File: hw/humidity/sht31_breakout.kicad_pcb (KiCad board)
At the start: 2 copper layers, 17.8 x 15.2 mm, 8 parts, among them P1 CONN_01X06, U1 SHT3x-DIS

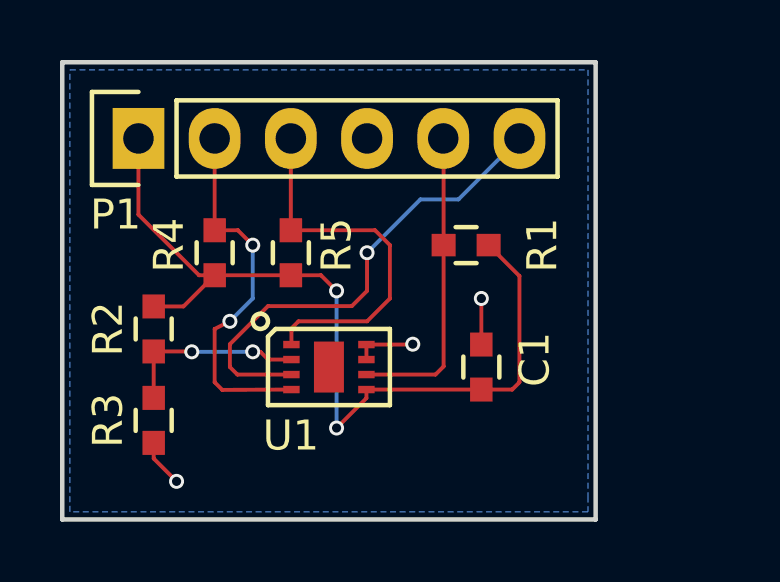
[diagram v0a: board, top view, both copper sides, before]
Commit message: Made much smaller SHT31 breakout
We'll see if I can hand solder it...
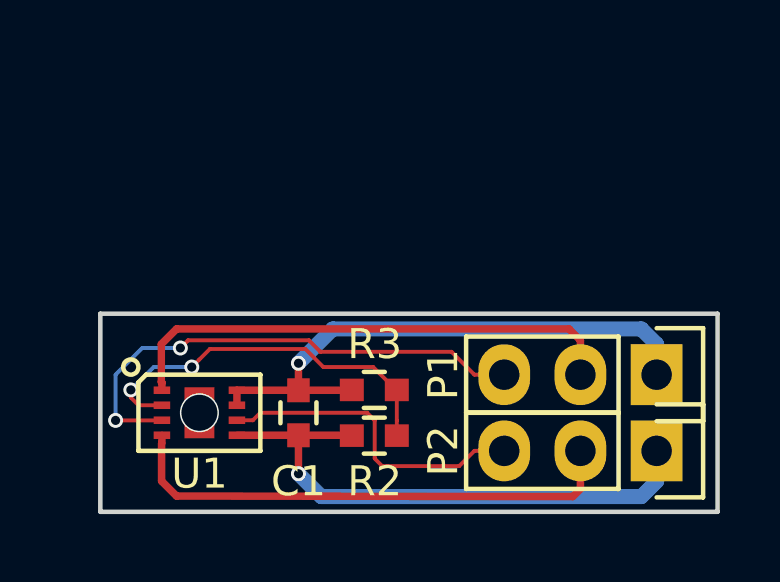
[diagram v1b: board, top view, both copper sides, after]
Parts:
- removed R1, R4, R5: 10k, Capacitors_SMD:C_0603
- added P2: CONN_01X03, Pin_Headers:Pin_Header_Straight_1x03, F.Cu at (160.8, 115.8)
- P1: value CONN_01X06 -> CONN_01X03; footprint Pin_Headers:Pin_Header_Straight_1x06 -> Pin_Headers:Pin_Header_Straight_1x03
- moved P1 19.0 mm to (160.8, 113.3), turned to 270 degrees
- moved R2 8.17 mm to (151.4, 115.3), turned to 0 degrees
- moved R3 7.42 mm to (151.4, 113.8), turned to 180 degrees
- moved C1 6.28 mm to (148.8, 114.6)
- moved U1 4.58 mm to (145.5, 114.6)
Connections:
- P1 pad 1: VDD -> GND
- P1 pad 2: /SCL -> /SDA
- P1 pad 3: /SDA -> /ALERT
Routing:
- net GND: track 5.18 -> 18.9 mm, vias 3 -> 1
- net VDD: track 29.1 -> 18.6 mm, vias 2 -> 1
- net /ADDR: track 6.25 -> 12.9 mm
- net /SCL: track 12.4 -> 17.1 mm, vias 2 -> 0
- net /SDA: track 12.6 -> 17.0 mm
- net /ALERT: track 16.2 -> 17.0 mm, vias 1 -> 2
- net (no net): vias 0 -> 1
- removed copper zone on B.Cu, net GND
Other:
- board size 17.8 x 15.2 mm -> 20.6 x 6.6 mm
- board text added: "ostur humidity 1.1"
- board text removed: "ostur humidity 1.0"

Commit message: Start designing flex pcb :D
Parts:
- removed P1, P2: CONN_01X03, Pin_Headers:Pin_Header_Straight_1x03
- added J1: CONN_01X04, footprints:smd_flex_4, F.Cu at (139.7, 124.5)
- moved C1 49.9 mm to (139.7, 65.5), turned to 180 degrees
- moved U1 46.3 mm to (139.7, 68.6), turned to 90 degrees
- moved R2 43.0 mm to (139.7, 73.9), turned to 180 degrees
- moved R3 43.0 mm to (139.7, 72.4)
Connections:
- U1 pad 3: /ALERT -> Net-(U1-Pad3)
- U1 pad 6: /nRESET -> VDD
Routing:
- net VDD: track 18.6 -> 63.7 mm, vias 1 -> 0
- net GND: track 18.9 -> 64.0 mm, vias 1 -> 0
- net /SCL: track 17.1 -> 55.7 mm, vias 0 -> 2
- net /SDA: track 17.0 -> 55.5 mm, vias 0 -> 2
- net /ALERT: track 17.0 -> 0.00 mm, vias 2 -> 0
- net /nRESET: track 10.7 -> 0.00 mm
- net /ADDR: track 12.9 -> 5.15 mm, vias 2 -> 0
- net (no net): vias 1 -> 0
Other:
- board size 20.6 x 6.6 mm -> 6.6 x 62.7 mm
- net class Default: clearance 0.16 -> 0.1524; trace_width 0.13 -> 0.1524; via_dia 0.5 -> 0.6858; via_drill 0.305 -> 0.3302
- rule trace_clearance: 0.16 -> 0.1524
- rule trace_min: 0.13 -> 0.1524
- rule via_min_drill: 0.305 -> 0.3302
- rule via_min_size: 0.5 -> 0.6858
- board text removed: "@alvaroprieto"
- board text removed: "ostur humidity 1.1"

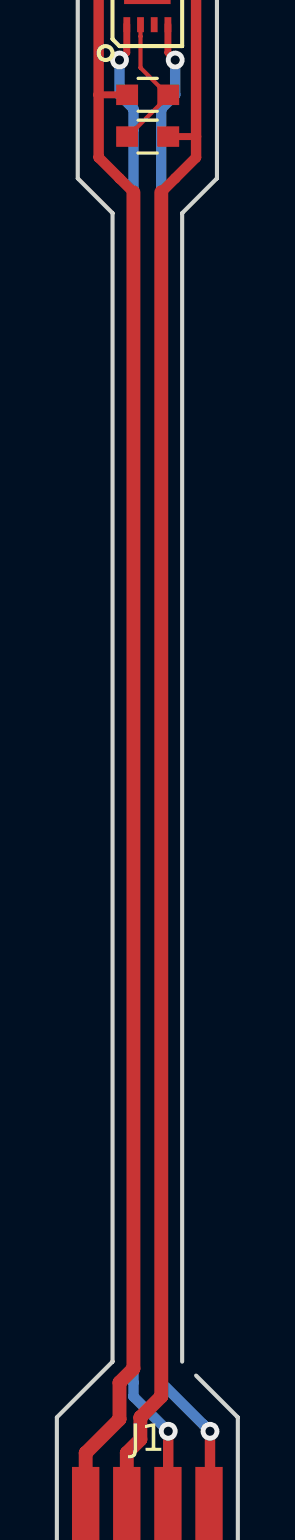
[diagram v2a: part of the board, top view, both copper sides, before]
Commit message: Added silkscreen and stiffener
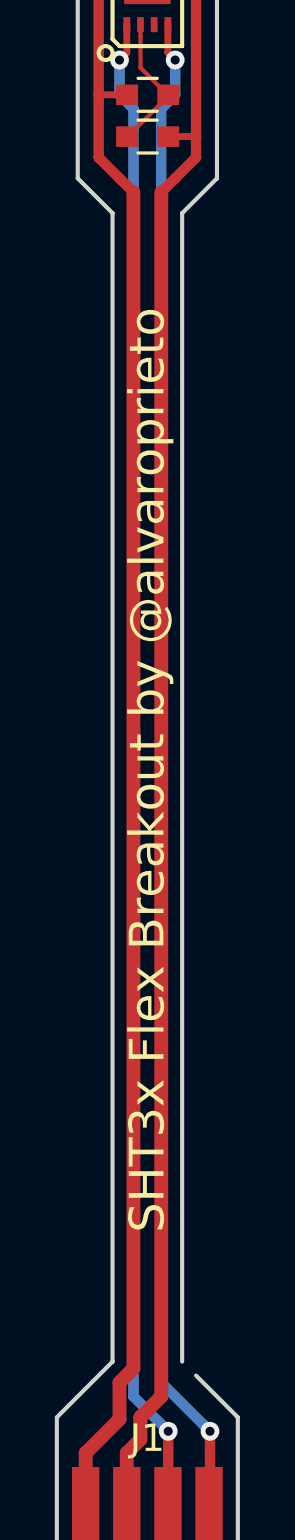
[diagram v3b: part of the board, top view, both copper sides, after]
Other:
- board text added: "SHT3x Flex Breakout by @alvaroprieto"
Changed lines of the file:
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@@
   (general
     (links 12)
-    (no_connects 1)
-    (area 0 0 0 0)
+    (no_connects 0)
+    (area 134.551267 63.0806 144.522734 127.075001)
     (thickness 1.6)
-    (drawings 12)
+    (drawings 13)
     (tracks 58)
     (zones 0)
@@
   )
   (setup
-    (last_trace_width 0.381)
+    (last_trace_width 0.1524)
     (user_trace_width 0.1524)
     (user_trace_width 0.254)
@@
     (pad 4 smd rect (at 2.25 0) (size 1 4) (layers F.Cu F.Paste F.Mask)
       (net 3 /SCL))
+  )
+  (gr_text "SHT3x Flex Breakout by @alvaroprieto" (at 139.7 97.028 90) (layer F.SilkS)
+    (effects (font (size 1.27 1.27) (thickness 0.254)))
   )
   (gr_line (start 137.16 75.438) (end 137.16 64.262) (layer Edge.Cuts) (width 0.15))
@@
   (segment (start 139.45 71.403) (end 139.45 70.2574) (width 0.1524) (layer F.Cu) (net 5))
   (segment (start 139.45 70.2574) (end 139.45 69.83) (width 0.1524) (layer F.Cu) (net 5))
+  (zone (net 0) (net_name "") (layer Eco1.User) (hatch edge 0.508)
+    (connect_pads (clearance 0.508))
+    (min_thickness 0.254)
+    (fill yes (arc_segments 16) (thermal_gap 0.508) (thermal_bridge_width 0.508))
+    (polygon
+      (pts
+        (xy 137.16 64.262) (xy 142.24 64.262) (xy 142.24 75.438) (xy 137.16 75.438)
+      )
+    )
+  )
 )

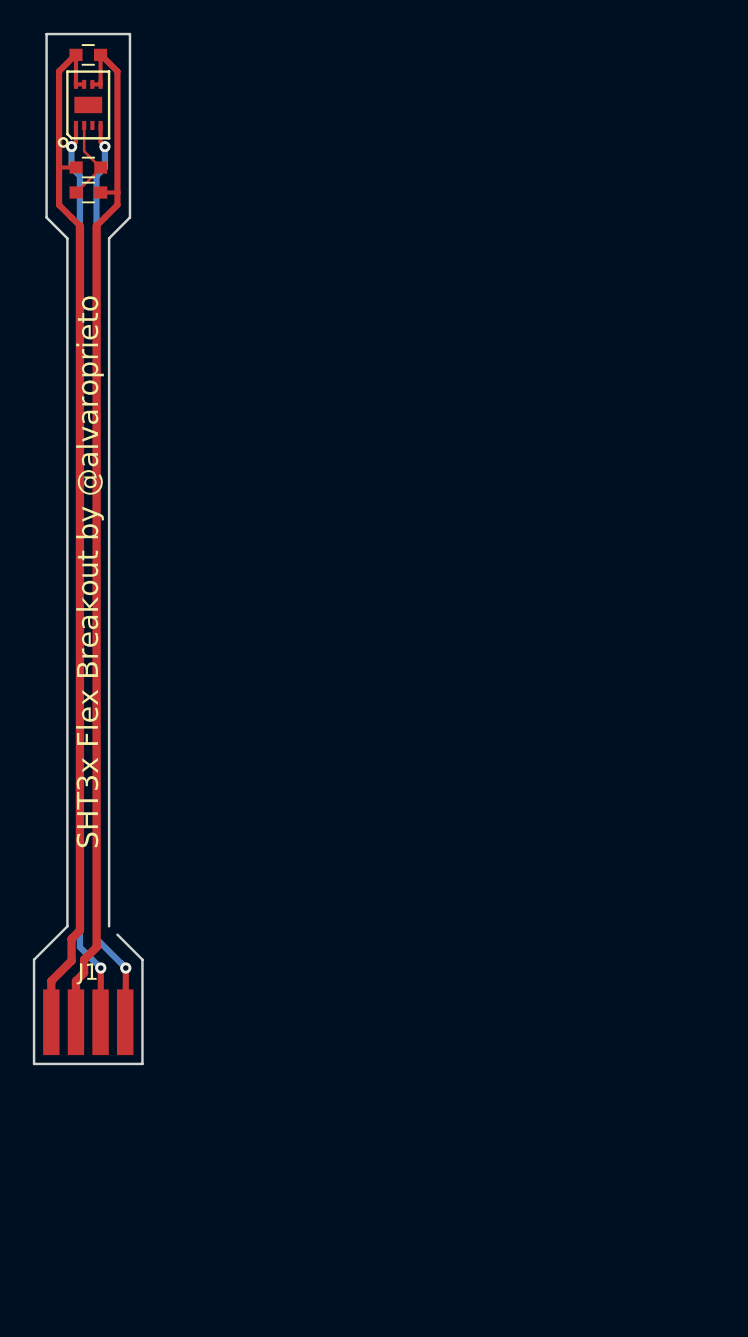
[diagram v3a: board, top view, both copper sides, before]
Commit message: Updated sht31 breakout to be wedge shaped!
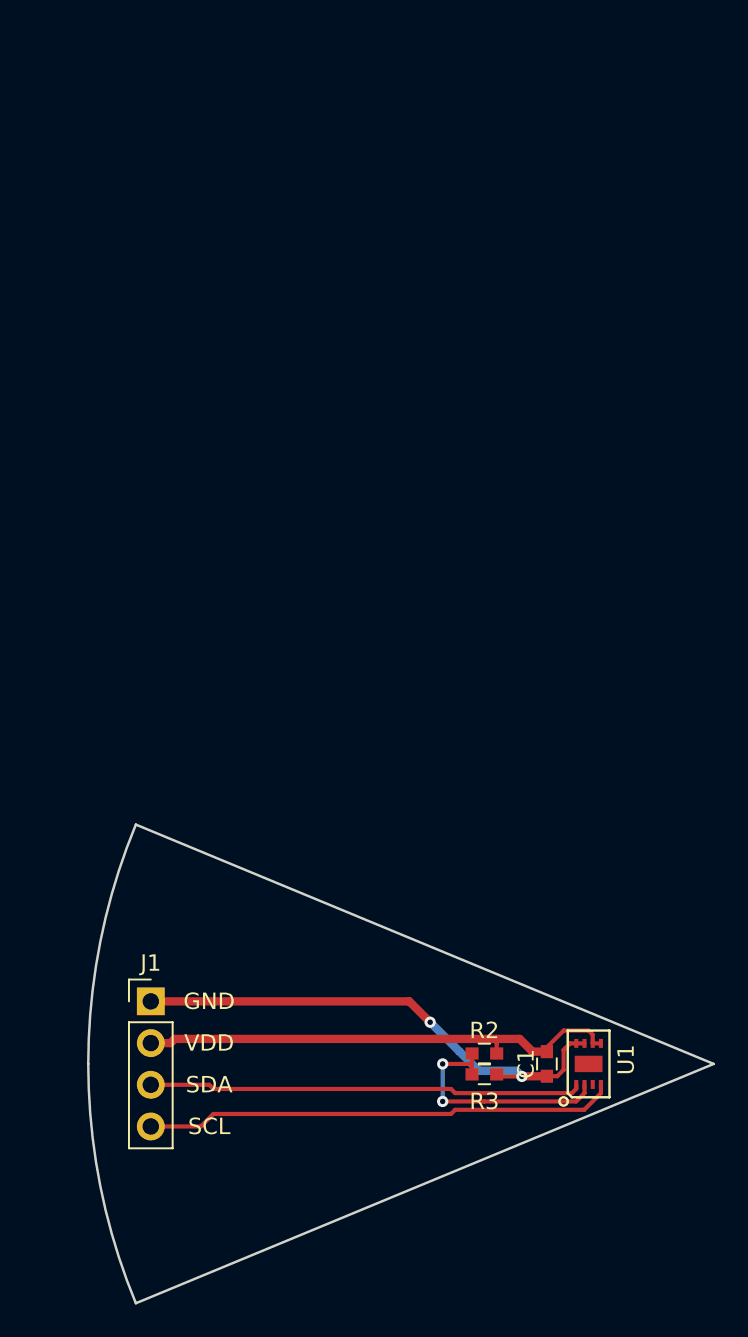
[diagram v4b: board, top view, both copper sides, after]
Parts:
- J1: footprint footprints:smd_flex_4 -> Pin_Headers:Pin_Header_Straight_1x04_Pitch2.54mm
- moved C1 67.5 mm to (167.6, 127.0), turned to 270 degrees
- moved U1 65.9 mm to (170.2, 127.0)
- moved R3 60.3 mm to (163.8, 127.6), turned to 0 degrees
- moved R2 57.7 mm to (163.8, 126.4)
- moved J1 4.02 mm to (143.5, 123.2)
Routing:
- net VDD: track 63.7 -> 30.2 mm
- net GND: track 64.0 -> 31.6 mm, vias 0 -> 2
- net /SDA: track 55.5 -> 26.5 mm, vias 2 -> 0
- net /SCL: track 55.7 -> 28.8 mm, vias 2 -> 0
- net /ADDR: track 5.15 -> 14.7 mm, vias 0 -> 2
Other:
- board size 6.6 x 62.7 mm -> 38.1 x 29.2 mm
- rule pad_to_mask_clearance: 0.2 -> 0.1016
- board text added: "GND"
- board text added: "Ostur T/H Sensor by @alvaroprieto"
- board text added: "SCL"
- board text added: "SDA"
- board text added: "VDD"
- board text removed: "SHT3x Flex Breakout by @alvaroprieto"

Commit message: Fixed silkscreens on controller/sensor
And submitted to pcbcart!
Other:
- board text added: "Humidity/Temperature"
- board text added: "Ostur"
- board text added: "by @alvaroprieto"
- board text removed: "Ostur T/H Sensor by @alvaroprieto"
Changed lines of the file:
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@@
   (general
     (links 12)
-    (no_connects 6)
-    (area 139.624999 112.34476 177.875001 141.65524)
+    (no_connects 0)
+    (area 138.524267 112.34476 177.875001 141.65524)
     (thickness 1.6)
-    (drawings 9)
+    (drawings 11)
     (tracks 59)
     (zones 0)
@@
   )
   (setup
-    (last_trace_width 0.254)
+    (last_trace_width 0.1524)
     (user_trace_width 0.1524)
     (user_trace_width 0.254)
@@
     (pcbplotparams
       (layerselection 0x010fc_80000001)
-      (usegerberextensions false)
+      (usegerberextensions true)
       (excludeedgelayer true)
       (linewidth 0.100000)
@@
     )
   )
-  (gr_text "Ostur T/H Sensor\nby @alvaroprieto" (at 147.32 127 90) (layer B.SilkS)
-    (effects (font (size 1 1) (thickness 0.15)) (justify mirror))
+  (gr_text Humidity/Temperature (at 156.1084 131.064 22.5) (layer B.SilkS)
+    (effects (font (size 1.5 1.5) (thickness 0.25)) (justify mirror))
+  )
+  (gr_text "by @alvaroprieto" (at 163.1188 130.9116 22.5) (layer B.SilkS)
+    (effects (font (size 1.5 1.5) (thickness 0.25)) (justify mirror))
+  )
+  (gr_text Ostur (at 154.2288 127.762 22.5) (layer B.SilkS)
+    (effects (font (size 3 3) (thickness 0.5)) (justify mirror))
   )
   (gr_text SCL (at 147.066 130.81) (layer F.SilkS)
